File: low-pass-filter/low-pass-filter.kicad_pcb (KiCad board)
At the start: 2 copper layers, 70.2 x 99.5 mm, 44 parts, among them J1 Power, J2 Power, J3 Pot, J4 CV, J5 Output, J6 Pot, J7 Input, J9 Pot, Q1 PNP, Q2 PNP, U1 LM13700, U2 TL074

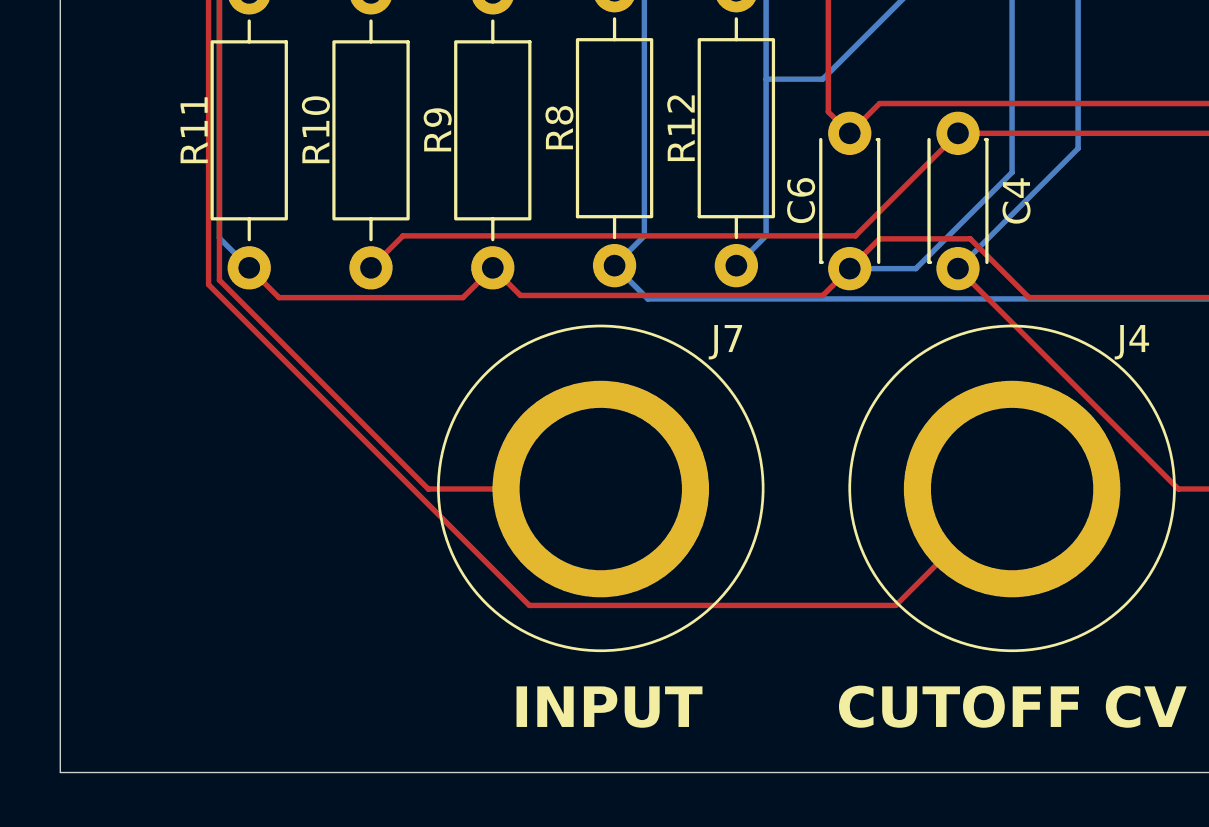
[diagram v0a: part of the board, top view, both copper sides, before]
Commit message: Add label to low-pass filter
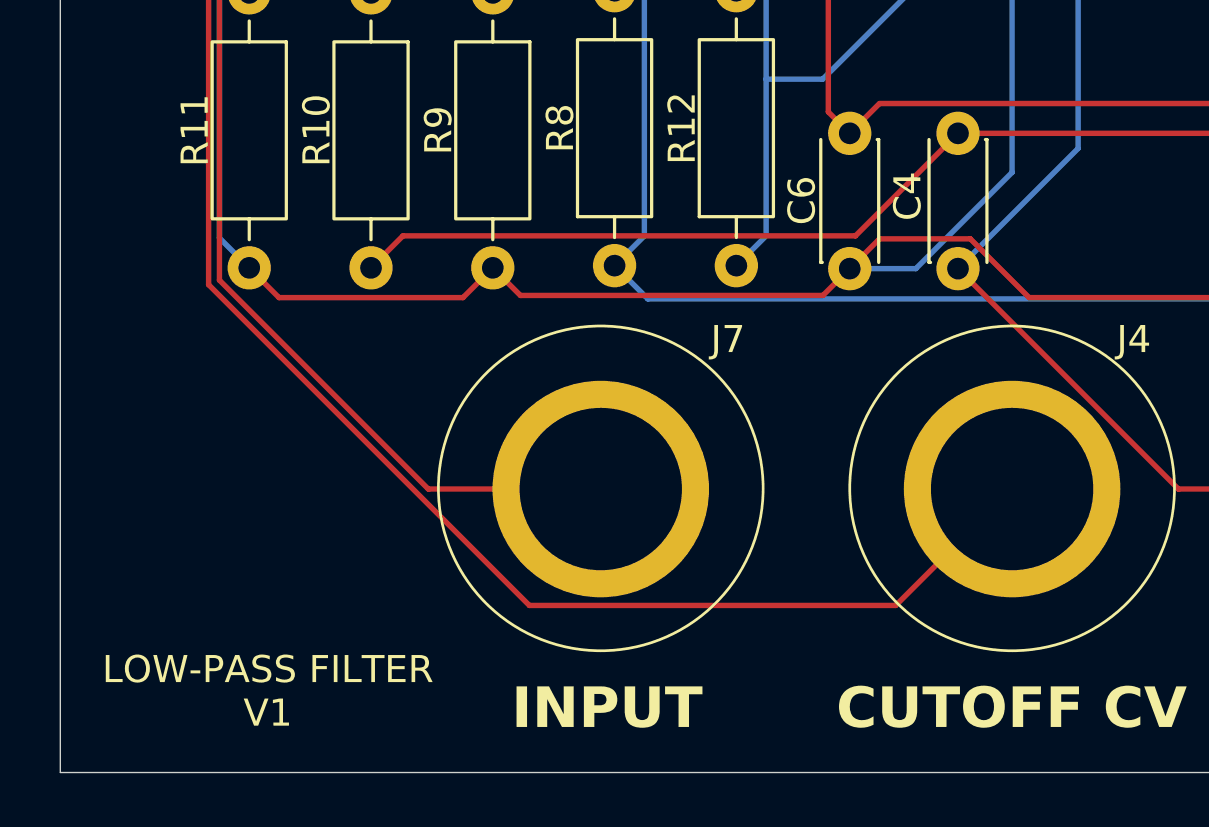
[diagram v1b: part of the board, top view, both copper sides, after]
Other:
- board text added: "LOW-PASS FILTER V1"
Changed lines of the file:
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@@
 			(outputformat 1)
 			(mirror no)
-			(drillshape 1)
+			(drillshape 0)
 			(scaleselection 1)
-			(outputdirectory "")
+			(outputdirectory "gerbers/")
 		)
 	)
@@
 		(tags "C Disc series Radial pin pitch 5.00mm diameter 4.3mm width 1.9mm Capacitor")
 		(property "Reference" "C4"
-			(at 2.5 -2.2 90)
+			(at 2.323249 1.852446 90)
 			(layer "F.SilkS")
 			(effects
@@
 		)
 	)
+	(gr_text "LOW-PASS FILTER\nV1"
+		(at 54 141 0)
+		(layer "F.SilkS")
+		(effects
+			(font
+				(size 1 1)
+				(thickness 0.1)
+			)
+		)
+	)

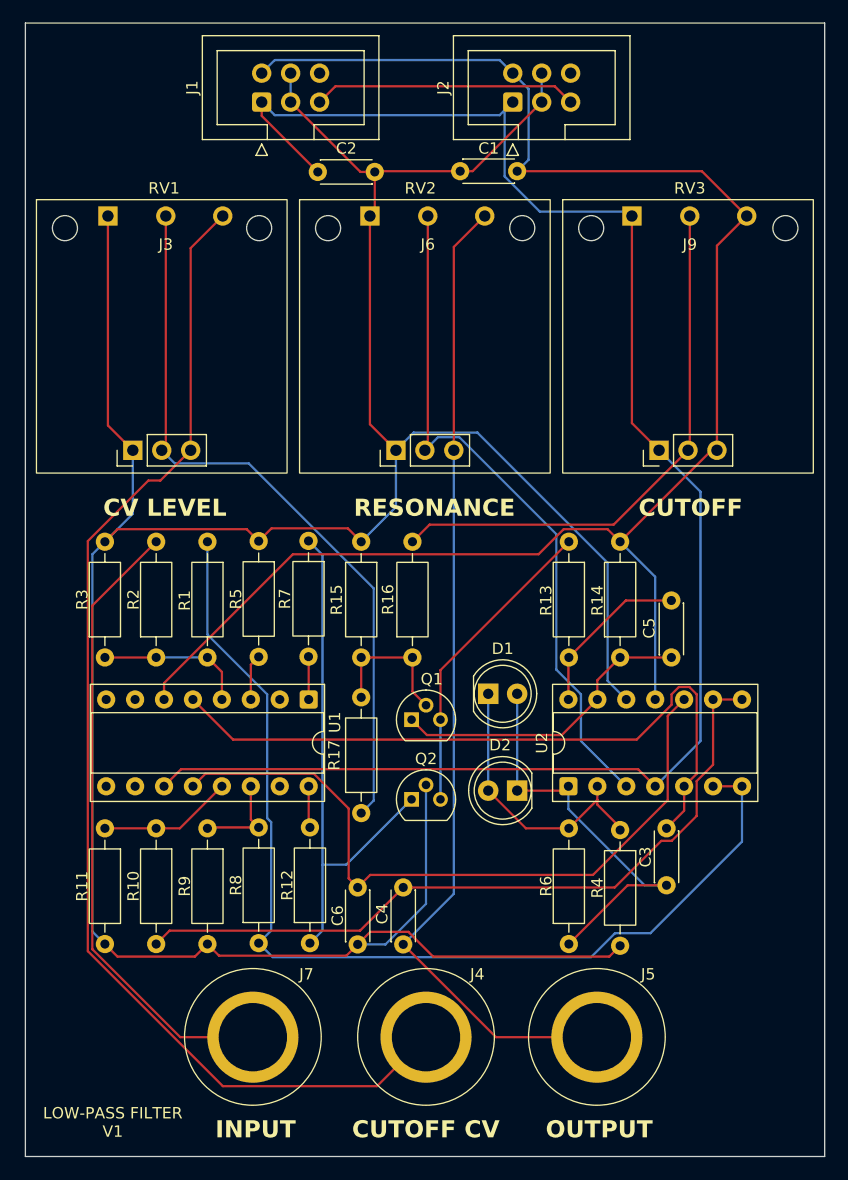
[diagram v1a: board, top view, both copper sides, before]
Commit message: More space for backup pot
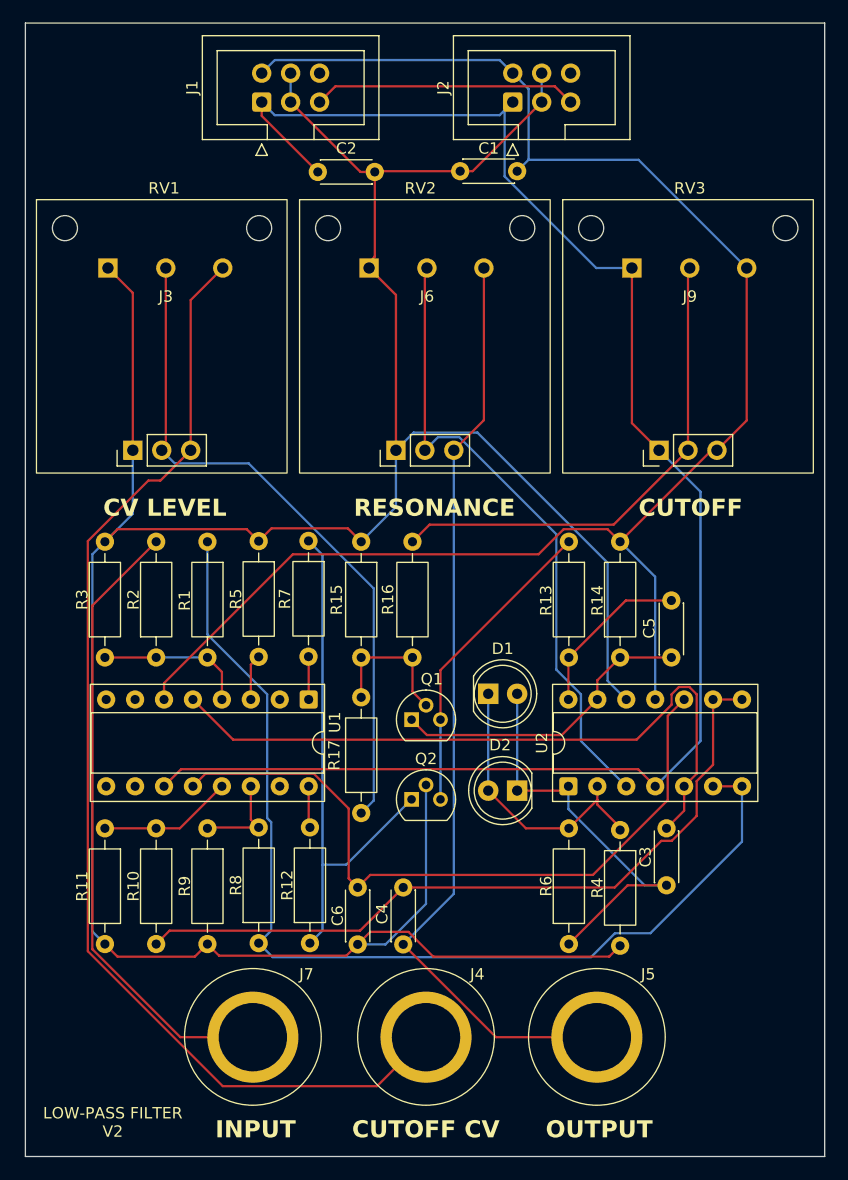
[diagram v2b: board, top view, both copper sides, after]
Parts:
- moved J6 4.57 mm to (81.6, 69.0)
- moved J3 4.56 mm to (58.7, 69.0)
- moved J9 4.56 mm to (104.7, 69.0)
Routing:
- net Net-(J5-Pin_1): track 87.3 -> 82.7 mm
- net Net-(J3-Pin_3): track 106.4 -> 101.9 mm
- net Net-(J3-Pin_2): track 64.5 -> 60.0 mm
- net GND: track 261.4 -> 256.9 mm
- net Net-(J9-Pin_2): track 48.1 -> 43.8 mm
- net Net-(J6-Pin_2): track 60.9 -> 56.7 mm
- net -12V: track 150.5 -> 147.2 mm
- net 12V: track 149.2 -> 146.5 mm
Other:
- board text added: "LOW-PASS FILTER V2"
- board text removed: "LOW-PASS FILTER V1"
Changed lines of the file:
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@@
 	(footprint "modular2:pot"
 		(layer "F.Cu")
-		(at 104.655001 64.435)
+		(at 104.655001 69)
 		(property "Reference" "J9"
 			(at 0 -0.5 0)
@@
 	(footprint "modular2:pot"
 		(layer "F.Cu")
-		(at 58.655001 64.435)
+		(at 58.655001 69)
 		(property "Reference" "J3"
 			(at 0 -0.5 0)
@@
 	(footprint "modular2:pot"
 		(layer "F.Cu")
-		(at 81.655001 64.435)
+		(at 81.58 69)
 		(property "Reference" "J6"
 			(at 0 -0.5 0)
@@
 		)
 	)
-	(gr_text "LOW-PASS FILTER\nV1"
+	(gr_text "LOW-PASS FILTER\nV2"
 		(at 54 141 0)
 		(layer "F.SilkS")
@@
 	)
 	(segment
-		(start 89.500001 57.5)
-		(end 105.720001 57.5)
-		(width 0.2)
-		(layer "F.Cu")
-		(net 1)
-	)
-	(segment
 		(start 58.500001 102.44295)
 		(end 69.811951 91.131)
@@
 	)
 	(segment
-		(start 107.040001 64.05)
-		(end 107.040001 82)
-		(width 0.2)
-		(layer "F.Cu")
-		(net 1)
-	)
-	(segment
-		(start 105.720001 57.5)
-		(end 109.655001 61.435)
-		(width 0.2)
-		(layer "F.Cu")
-		(net 1)
-	)
-	(segment
 		(start 93.583951 88.928043)
 		(end 97.439001 88.928043)
@@
 	)
 	(segment
-		(start 109.655001 61.435)
-		(end 107.040001 64.05)
+		(start 107.040001 82)
+		(end 109.655001 79.385)
 		(width 0.2)
 		(layer "F.Cu")
@@
 	)
 	(segment
+		(start 109.655001 79.385)
+		(end 109.655001 66)
+		(width 0.2)
+		(layer "F.Cu")
+		(net 1)
+	)
+	(segment
 		(start 107.040001 82)
 		(end 106.569044 82)
@@
 	)
 	(segment
+		(start 109.655001 66)
+		(end 100.155001 56.5)
+		(width 0.2)
+		(layer "B.Cu")
+		(net 1)
+	)
+	(segment
 		(start 89.115001 48.895)
 		(end 90.500001 50.28)
@@
 	)
 	(segment
+		(start 100.155001 56.5)
+		(end 90.500001 56.5)
+		(width 0.2)
+		(layer "B.Cu")
+		(net 1)
+	)
+	(segment
 		(start 87.964001 47.744)
 		(end 89.115001 48.895)
@@
 	)
 	(segment
-		(start 77.000001 57.566085)
-		(end 77.000001 61.01)
+		(start 76.5 65.5)
+		(end 77.000001 64.999999)
 		(width 0.2)
 		(layer "F.Cu")
@@
 	)
 	(segment
-		(start 76.575001 61.435)
-		(end 76.575001 79.715)
-		(width 0.2)
-		(layer "F.Cu")
-		(net 2)
-	)
-	(segment
-		(start 53.575001 61.435)
-		(end 53.575001 79.815)
+		(start 78.860001 68.360001)
+		(end 76.5 66)
 		(width 0.2)
 		(layer "F.Cu")
@@
 	)
 	(segment
+		(start 55.760001 68.185)
+		(end 53.575001 66)
+		(width 0.2)
+		(layer "F.Cu")
+		(net 2)
+	)
+	(segment
+		(start 76.5 66)
+		(end 76.5 65.5)
+		(width 0.2)
+		(layer "F.Cu")
+		(net 2)
+	)
+	(segment
 		(start 62.310001 125.35)
 		(end 63.331001 126.371)
@@
 	)
 	(segment
-		(start 75.746086 57.566085)
-		(end 77.000001 57.566085)
+		(start 55.760001 82)
+		(end 55.760001 68.185)
 		(width 0.2)
 		(layer "F.Cu")
@@
 	)
 	(segment
-		(start 76.575001 79.715)
-		(end 78.860001 82)
+		(start 75.746086 57.566085)
+		(end 77.000001 57.566085)
 		(width 0.2)
 		(layer "F.Cu")
@@
 	)
 	(segment
-		(start 53.575001 79.815)
-		(end 55.760001 82)
-		(width 0.2)
-		(layer "F.Cu")
-		(net 2)
-	)
-	(segment
 		(start 53.310001 125.35)
 		(end 54.411001 126.451)
@@
 	)
 	(segment
+		(start 78.860001 82)
+		(end 78.860001 68.360001)
+		(width 0.2)
+		(layer "F.Cu")
+		(net 2)
+	)
+	(segment
+		(start 77.000001 64.999999)
+		(end 77.000001 57.566085)
+		(width 0.2)
+		(layer "F.Cu")
+		(net 2)
+	)
+	(segment
 		(start 69.615001 51.435)
 		(end 75.746086 57.566085)
@@
 	)
 	(segment
-		(start 77.000001 61.01)
-		(end 76.575001 61.435)
-		(width 0.2)
-		(layer "F.Cu")
-		(net 2)
-	)
-	(segment
 		(start 74.509001 126.371)
 		(end 75.500001 125.38)
@@
 	)
 	(segment
+		(start 99.575001 79.615)
+		(end 101.960001 82)
+		(width 0.2)
+		(layer "F.Cu")
+		(net 3)
+	)
+	(segment
 		(start 60.002001 109.998)
 		(end 58.500001 111.5)
@@
 	)
 	(segment
-		(start 99.575001 79.615)
-		(end 101.960001 82)
+		(start 99.575001 66)
+		(end 99.575001 79.615)
 		(width 0.2)
 		(layer "F.Cu")
@@
 	)
 	(segment
-		(start 99.575001 61.435)
-		(end 99.575001 79.615)
-		(width 0.2)
-		(layer "F.Cu")
-		(net 3)
-	)
-	(segment
 		(start 101.620001 111.5)
 		(end 100.118001 109.998)
@@
 	)
 	(segment
-		(start 88.399001 57.95605)
-		(end 91.491951 61.049)
-		(width 0.2)
-		(layer "B.Cu")
-		(net 3)
-	)
-	(segment
 		(start 101.960001 82)
 		(end 105.599001 85.639)
@@
 	)
 	(segment
-		(start 99.189001 61.049)
-		(end 99.575001 61.435)
-		(width 0.2)
-		(layer "B.Cu")
-		(net 3)
-	)
-	(segment
 		(start 89.115001 51.435)
 		(end 88.399001 52.151)
@@
 	)
 	(segment
-		(start 88.399001 52.151)
-		(end 88.399001 57.95605)
+		(start 99.575001 66)
+		(end 96.442951 66)
 		(width 0.2)
 		(layer "B.Cu")
@@
 	)
 	(segment
-		(start 91.491951 61.049)
-		(end 99.189001 61.049)
+		(start 88.399001 52.151)
+		(end 88.399001 57.95605)
 		(width 0.2)
 		(layer "B.Cu")
@@
 	)
 	(segment
+		(start 96.442951 66)
+		(end 88.399001 57.95605)
+		(width 0.2)
+		(layer "B.Cu")
+		(net 3)
+	)
+	(segment
 		(start 64.561001 107.401)
 		(end 99.994051 107.401)
@@
 	)
 	(segment
-		(start 83.940001 64.15)
-		(end 83.940001 82)
+		(start 86.58 79.360001)
+		(end 86.58 66)
 		(width 0.2)
 		(layer "F.Cu")
@@
 	)
 	(segment
-		(start 86.655001 61.435)
-		(end 83.940001 64.15)
+		(start 83.940001 82)
+		(end 86.58 79.360001)
 		(width 0.2)
 		(layer "F.Cu")
@@
 	)
 	(segment
-		(start 58.655001 61.435)
+		(start 58.655001 66)
 		(end 58.655001 81.645)
 		(width 0.2)
@@
 	)
 	(segment
+		(start 60.840001 68.815)
+		(end 63.655001 66)
+		(width 0.2)
+		(layer "F.Cu")
+		(net 16)
+	)
+	(segment
 		(start 57.122951 84.66)
 		(end 51.808001 89.97495)
@@
 	)
 	(segment
-		(start 63.655001 61.435)
-		(end 60.840001 64.25)
+		(start 60.840001 82)
+		(end 60.840001 68.815)
 		(width 0.2)
 		(layer "F.Cu")
@@
 	)
 	(segment
-		(start 60.840001 64.25)
-		(end 60.840001 82)
+		(start 81.400001 82)
+		(end 81.400001 66.179999)
 		(width 0.2)
 		(layer "F.Cu")
-		(net 16)
+		(net 17)
 	)
 	(segment
-		(start 81.655001 61.435)
-		(end 81.655001 81.745)
+		(start 81.400001 66.179999)
+		(end 81.58 66)
 		(width 0.2)
 		(layer "F.Cu")
@@
 	)
 	(segment
+		(start 104.500001 66.155)
+		(end 104.655001 66)
+		(width 0.2)
+		(layer "F.Cu")
+		(net 19)
+	)
+	(segment
 		(start 104.655001 81.845)
 		(end 104.500001 82)
@@
 	)
 	(segment
-		(start 81.812958 88.527043)
-		(end 80.310001 90.03)
+		(start 104.500001 82)
+		(end 104.500001 66.155)
 		(width 0.2)
 		(layer "F.Cu")
@@
 	)
 	(segment
-		(start 104.500001 82)
-		(end 97.972958 88.527043)
+		(start 81.812958 88.527043)
+		(end 80.310001 90.03)
 		(width 0.2)
 		(layer "F.Cu")
@@
 	)
 	(segment
-		(start 104.655001 61.435)
-		(end 104.655001 81.845)
+		(start 104.500001 82)
+		(end 97.972958 88.527043)
 		(width 0.2)
 		(layer "F.Cu")

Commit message: Various improvements
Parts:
- added C7: 100nf, Capacitor_THT:C_Disc_D4.3mm_W1.9mm_P5.00mm, F.Cu at (50.5, 106.5)
- added C8: 100nf, Capacitor_THT:C_Disc_D4.3mm_W1.9mm_P5.00mm, F.Cu at (50.5, 114.0)
- added G***: LOGO, modular2:ibis-small, F.Cu at (112.5, 139.0)
- moved C1 59.4 mm to (106.6, 114.4)
- moved C2 50.0 mm to (101.6, 101.1), turned to 0 degrees
- moved C5 2.19 mm to (103.0, 93.0)
- moved C3 1.86 mm to (101.8, 121.8)
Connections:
- C1 pad 1: -12V -> GND
- C1 pad 2: GND -> 12V
- C2 pad 1: GND -> -12V
- C2 pad 2: 12V -> GND
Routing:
- net GND: track 256.9 -> 287.9 mm
- net 12V: track 146.5 -> 157.5 mm
- net -12V: track 147.2 -> 154.8 mm
- net Net-(U2B-+): track 61.3 -> 63.3 mm
- net Net-(D1-A): track 37.3 -> 35.9 mm
- net Net-(U2C-+): track 62.5 -> 63.7 mm
- net Net-(C5-Pad1): track 14.8 -> 15.7 mm
- net Net-(Q1-C): track 27.2 -> 28.1 mm

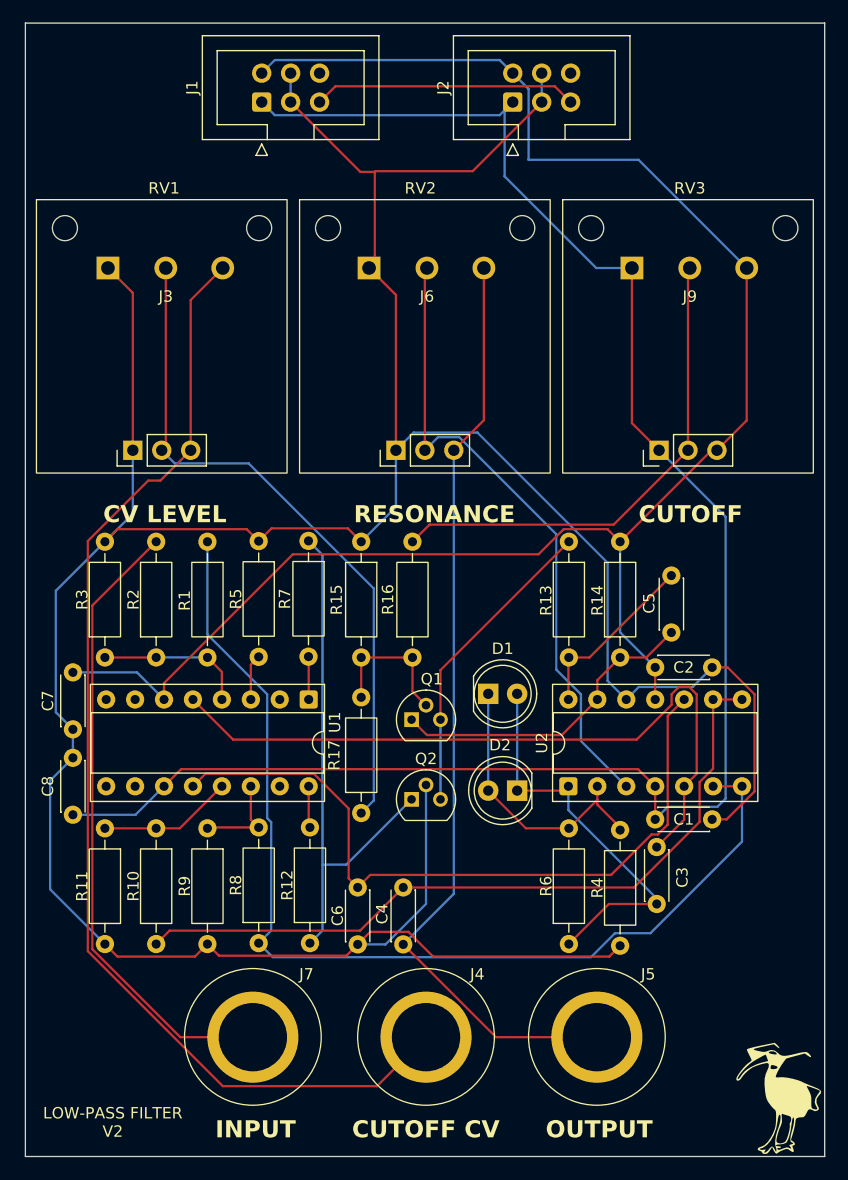
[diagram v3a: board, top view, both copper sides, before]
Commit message: Update low-pass filter
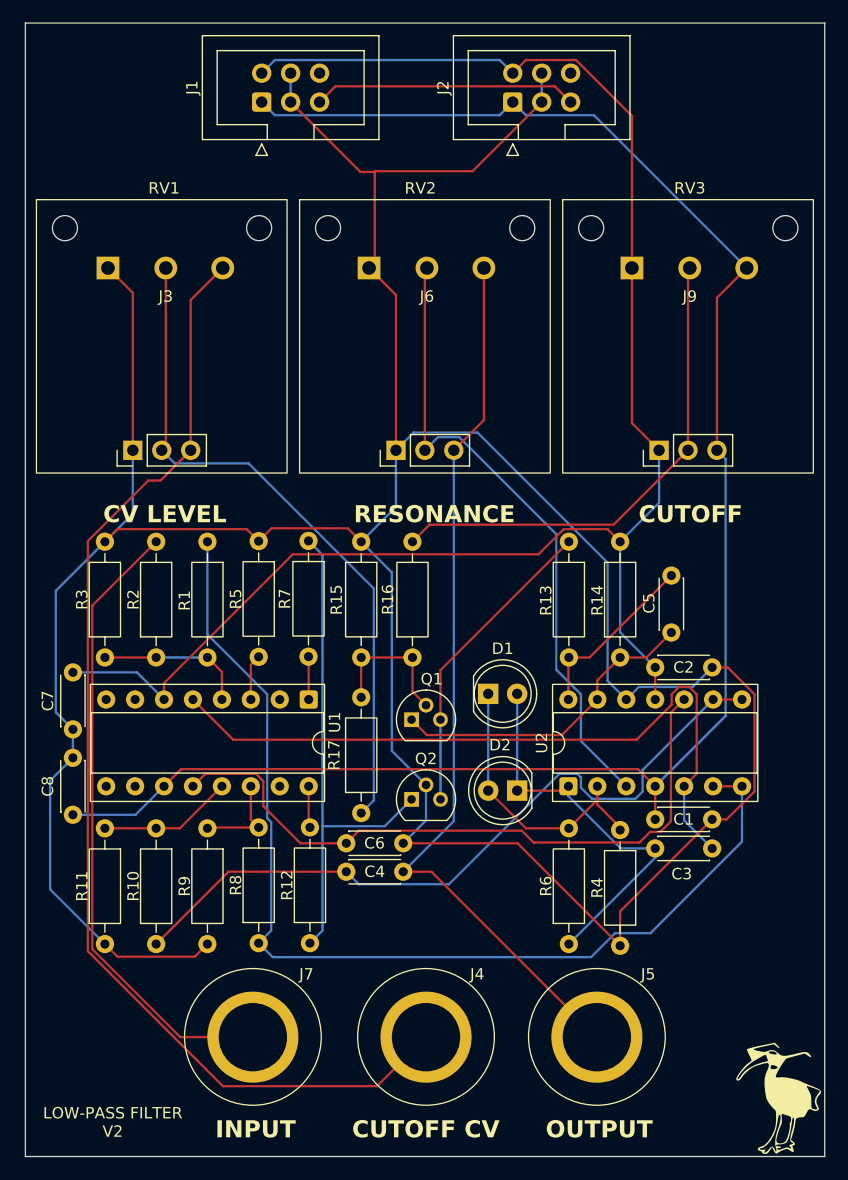
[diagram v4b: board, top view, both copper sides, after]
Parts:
- Q1, Q2: value PNP -> PNP (e.g. BC558)
- moved C6 9.74 mm to (79.5, 116.5), turned to 180 degrees
- moved C4 5.19 mm to (74.5, 119.0), turned to 0 degrees
- moved C3 4.88 mm to (101.6, 117.0), turned to 0 degrees
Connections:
- J9 pad 1: 12V -> -12V
- J9 pad 3: -12V -> 12V
- RV3 pad 1: 12V -> -12V
- RV3 pad 3: -12V -> 12V
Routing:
- net GND: track 287.9 -> 298.0 mm
- net -12V: track 154.8 -> 147.4 mm
- net Net-(U2C-+): track 63.7 -> 59.1 mm
- net Net-(J5-Pin_1): track 82.7 -> 78.9 mm
- net 12V: track 157.5 -> 155.3 mm
- net Net-(Q2-C): track 46.5 -> 45.1 mm
- net Net-(U2C--): track 65.9 -> 64.7 mm
- net Net-(D1-A): track 35.9 -> 35.1 mm

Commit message: Various fixes
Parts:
- added J8: Power, Connector_IDC:IDC-Header_2x03_P2.54mm_Vertical, F.Cu at (96.5, 51.5)
- moved J2 10.1 mm to (79.0, 51.5)
- moved J1 5.66 mm to (61.4, 51.4)
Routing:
- net GND: track 298.0 -> 318.4 mm
- net 5V: track 23.2 -> 36.9 mm
- net 12V: track 155.3 -> 163.0 mm
- net -12V: track 147.4 -> 154.3 mm
